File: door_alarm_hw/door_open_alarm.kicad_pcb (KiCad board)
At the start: 2 copper layers, 57.7 x 48.1 mm, 59 parts, among them J1 TYPE-C 16PIN 2MD(073), Q1 BSS138PW,115, Q2 CJ2301 S1, Q3 CJ2301 S1, U1 AP2114HA-3.3TRG1, U2 ESP32-S3-MINI-1

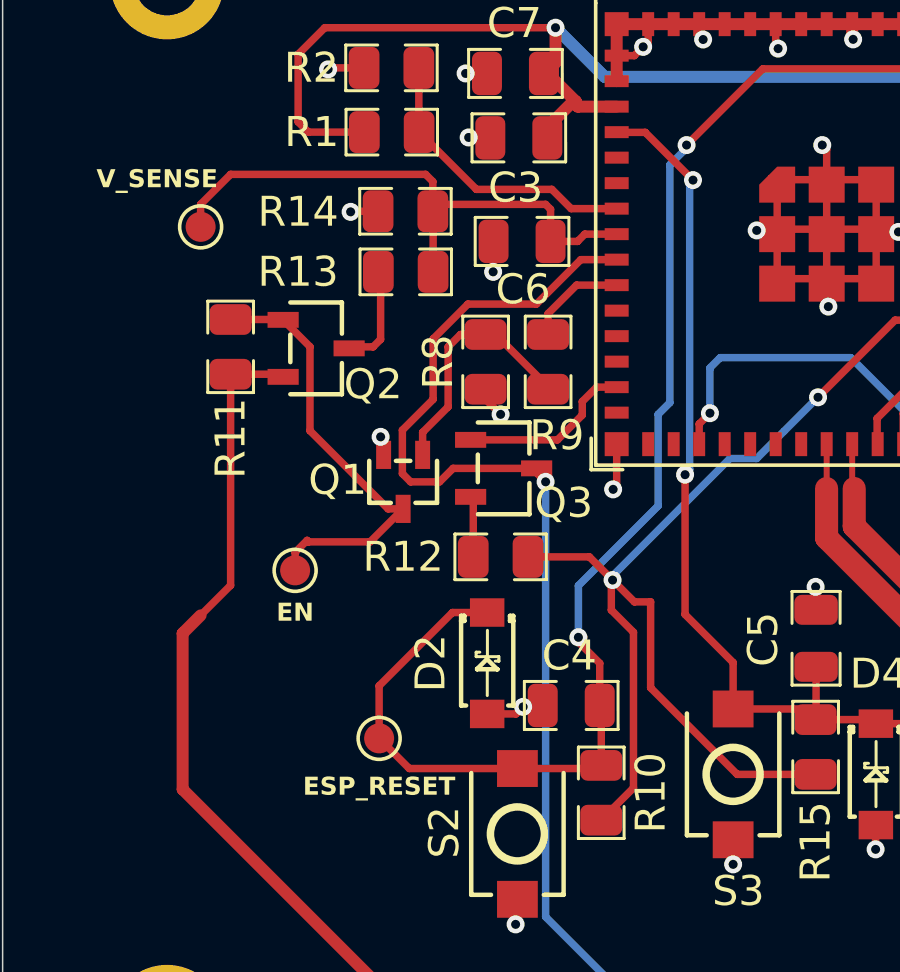
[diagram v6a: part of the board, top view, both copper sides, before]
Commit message: Resistor mix up fix, label fix
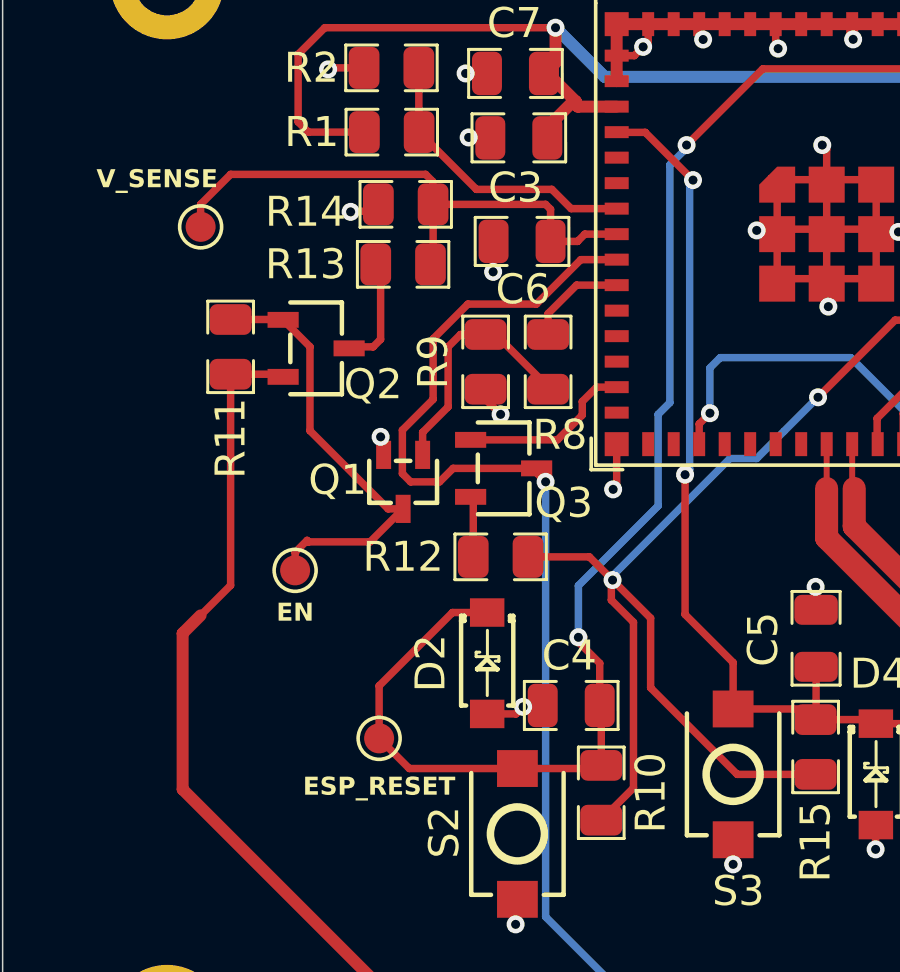
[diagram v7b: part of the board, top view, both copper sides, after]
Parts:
- R13: value 0805W8F5101T5E -> 0805W8J0203T5E
- R14: value 0805W8J0203T5E -> 0805W8F5101T5E
- moved R13 0.26 mm to (95.2, 78.5)
- moved R14 0.23 mm to (95.3, 76.5)
